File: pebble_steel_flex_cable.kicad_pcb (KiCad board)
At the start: 2 copper layers, 80 x 19 mm, 33 parts, among them J1 505551-1620, SW1 Select, SW2 DOWN, SW3 UP, SW4 BACK, U1 IS31FL3199-QFLS2-TR

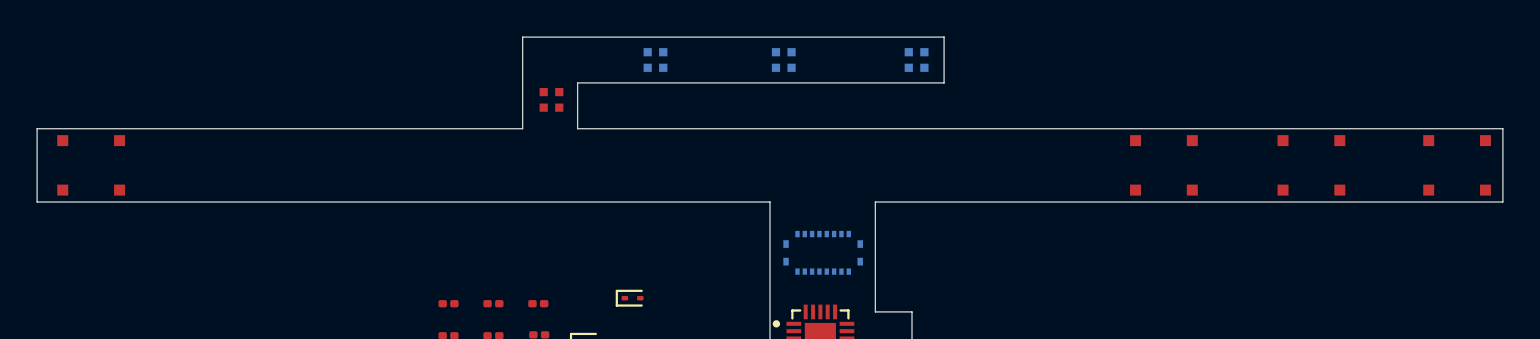
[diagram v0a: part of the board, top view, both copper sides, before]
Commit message: added the buttons and the battery connections
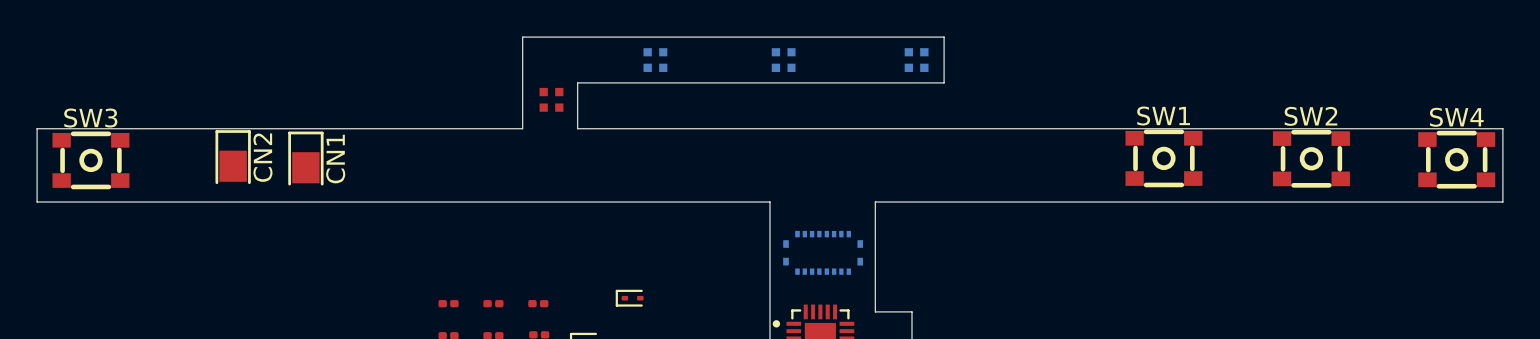
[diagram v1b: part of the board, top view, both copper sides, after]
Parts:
- added CN1: ~, S7121-42R:SMD_L2.7-W1.5, F.Cu at (108.7, 58.1)
- added CN2: ~, S7121-42R:SMD_L2.7-W1.5, F.Cu at (104.7, 58.0)
- SW1: value Select -> UP; footprint button-TL3315NF250Q:SW_TL3315NF250Q -> SKSHAAE010:SW-SMD_SKSHAAE010
- SW2: value DOWN -> Select; footprint button-TL3315NF250Q:SW_TL3315NF250Q -> SKSHAAE010:SW-SMD_SKSHAAE010
- SW3: value UP -> Back; footprint button-TL3315NF250Q:SW_TL3315NF250Q -> SKSHAAE010:SW-SMD_SKSHAAE010
- SW4: value BACK -> Down; footprint button-TL3315NF250Q:SW_TL3315NF250Q -> SKSHAAE010:SW-SMD_SKSHAAE010
- moved SW4 74.5 mm to (171.5, 57.7)
- moved SW3 58.6 mm to (96.9, 57.7)
- moved SW1 16.0 mm to (155.5, 57.6)
- moved SW2 0.36 mm to (163.6, 57.6)
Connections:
- SW1 pad 2: Net-(D3-A2) -> unconnected-(SW1-Pad2)
- SW1 pad 3: (no net) -> unconnected-(SW1-Pad3)
- SW1 pad 4: (no net) -> Net-(D3-A2)
- SW2 pad 2: Net-(D4-A2) -> unconnected-(SW2-Pad2)
- SW2 pad 3: (no net) -> unconnected-(SW2-Pad3)
- SW2 pad 4: (no net) -> Net-(D4-A2)
- SW3 pad 2: Net-(D2-A2) -> unconnected-(SW3-Pad2)
- SW3 pad 3: (no net) -> unconnected-(SW3-Pad3)
- SW3 pad 4: (no net) -> Net-(D2-A2)
- SW4 pad 2: Net-(D5-A2) -> unconnected-(SW4-Pad2)
- SW4 pad 3: (no net) -> unconnected-(SW4-Pad3)
- SW4 pad 4: (no net) -> Net-(D5-A2)

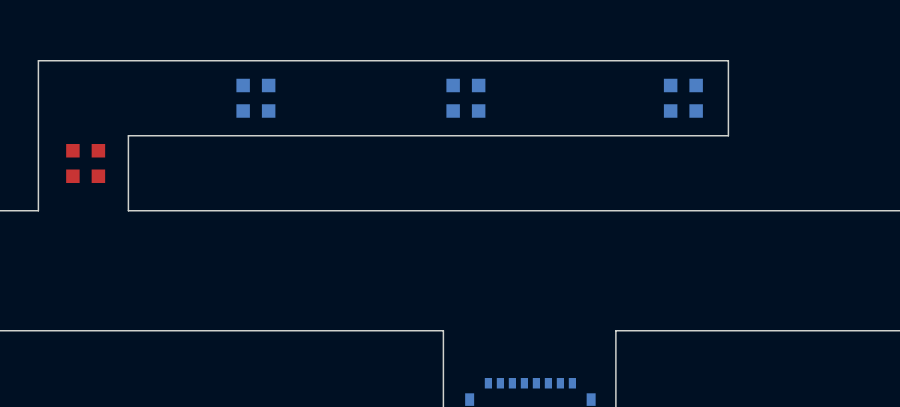
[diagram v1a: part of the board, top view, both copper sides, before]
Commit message: added the LED part
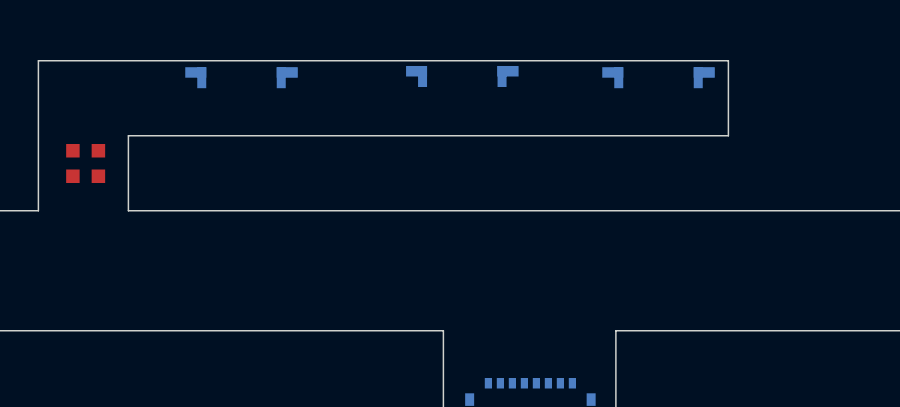
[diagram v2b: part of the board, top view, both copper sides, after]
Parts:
- CN1: value ~ -> 5v
- CN2: value ~ -> GND
- D6, D7, D8: footprint footprints:led_SML-LX0404SIUPGUSB -> LTW-020ZDCG:LTW-020ZDCG
- moved D8 3.75 mm to (141.2, 48.6)
- moved D7 3.70 mm to (134.6, 48.5)
- moved D6 3.69 mm to (127.3, 48.6)

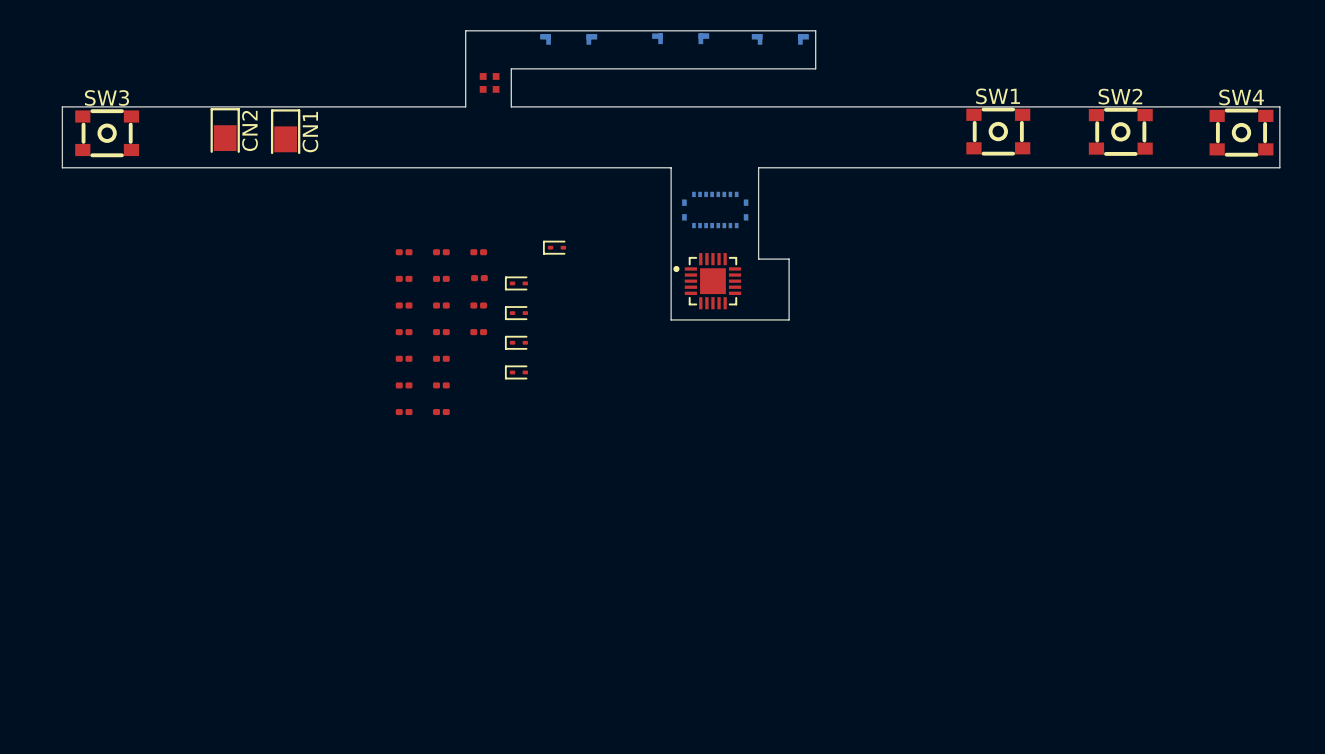
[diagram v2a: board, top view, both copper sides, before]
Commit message: got the outline almost there
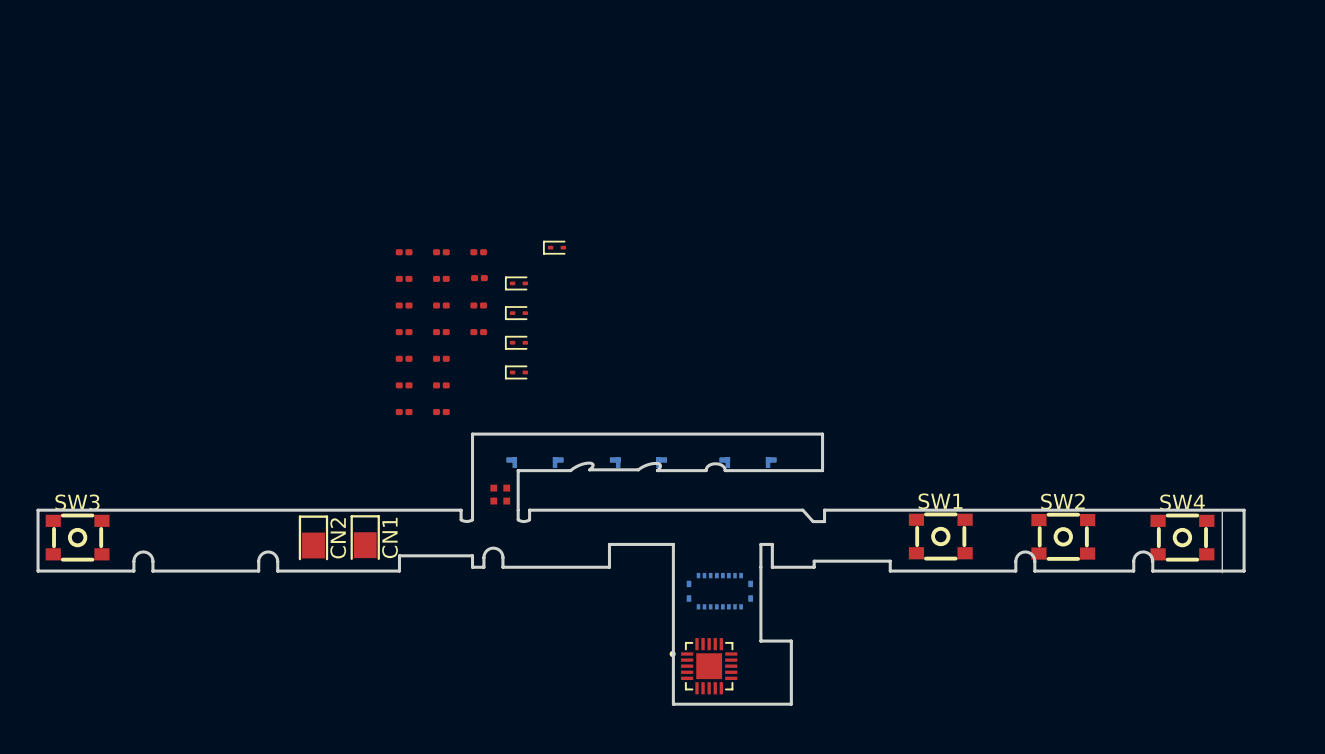
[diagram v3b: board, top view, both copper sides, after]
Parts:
- moved D7 28.0 mm to (131.8, 76.4)
- moved D6 27.9 mm to (125.0, 76.4)
- moved D8 27.9 mm to (139.1, 76.4)
- moved CN2 27.4 mm to (110.5, 84.8)
- moved CN1 27.2 mm to (113.9, 84.8)
- moved D10 27.1 mm to (122.8, 81.5)
- moved SW4 26.9 mm to (167.6, 84.3)
- moved SW1 26.9 mm to (151.7, 84.2)
- moved SW2 26.9 mm to (159.8, 84.2)
- moved SW3 26.6 mm to (95.0, 84.3)
- moved U1 25.3 mm to (136.5, 92.8)
- moved J1 25.1 mm to (137.2, 87.8)
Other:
- board size 80 x 19 mm -> 79.2 x 17.8 mm

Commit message: got the flex layed out
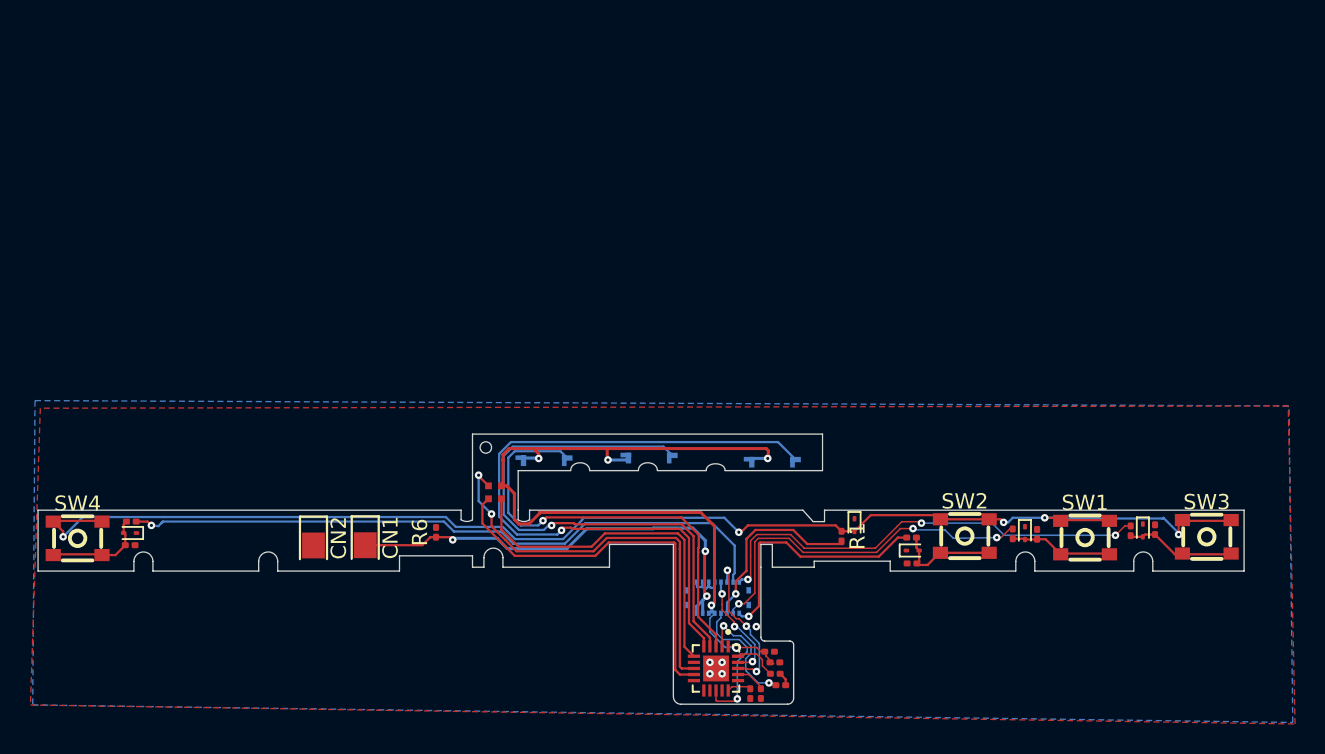
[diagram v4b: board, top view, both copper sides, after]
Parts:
- removed C5, C6: C, Capacitor_SMD:C_0201_0603Metric
- SW1: value UP -> Select
- SW2: value Select -> UP
- SW3: value Back -> Down
- SW4: value Down -> Back
- moved SW3 74.2 mm to (169.2, 84.2)
- moved SW4 72.6 mm to (95.0, 84.3)
- moved C4 51.0 mm to (165.8, 83.8), turned to 90 degrees
- moved R5 46.6 mm to (164.2, 83.9), turned to -90 degrees
- moved C3 44.2 mm to (158.1, 84.1), turned to 90 degrees
- moved D5 42.3 mm to (165.0, 83.8), turned to -90 degrees
- moved R4 38.4 mm to (156.4, 84.1), turned to -90 degrees
- moved C2 38.3 mm to (149.8, 86.0), turned to 180 degrees
- moved C9 36.1 mm to (141.2, 94.0)
- moved D4 35.5 mm to (157.2, 84.0), turned to -90 degrees
- moved C10 33.4 mm to (140.8, 92.5)
- moved R3 32.5 mm to (149.8, 84.3)
- moved C11 31.3 mm to (140.5, 91.8)
- moved R7 31.1 mm to (139.2, 94.6), turned to 90 degrees
- moved D2 30.4 mm to (98.4, 84.0), turned to 180 degrees
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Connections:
- R2 pad 1: Net-(J1-Pad2) -> Net-(J1-Pad4)
- R5 pad 1: Net-(J1-Pad4) -> Net-(J1-Pad2)
- R6 pad 1: +3.3V -> +5V
- SW1 pad 2: unconnected-(SW1-Pad2) -> Net-(D4-A2)
- SW1 pad 3: unconnected-(SW1-Pad3) -> Net-(D1-A2)
- SW1 pad 4: Net-(D3-A2) -> Net-(D4-A2)
- SW2 pad 2: unconnected-(SW2-Pad2) -> Net-(D3-A2)
- SW2 pad 3: unconnected-(SW2-Pad3) -> Net-(D1-A2)
- SW2 pad 4: Net-(D4-A2) -> Net-(D3-A2)
- SW3 pad 2: unconnected-(SW3-Pad2) -> Net-(D5-A2)
- SW3 pad 3: unconnected-(SW3-Pad3) -> Net-(D1-A2)
- SW3 pad 4: Net-(D2-A2) -> Net-(D5-A2)
- SW4 pad 2: unconnected-(SW4-Pad2) -> Net-(D2-A2)
- SW4 pad 3: unconnected-(SW4-Pad3) -> Net-(D1-A2)
- SW4 pad 4: Net-(D5-A2) -> Net-(D2-A2)
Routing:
- net Net-(D1-A2): track 0.00 -> 90.3 mm, vias 0 -> 5
- net +3.3V: track 0.00 -> 55.9 mm, vias 0 -> 5
- net /LED3: track 0.00 -> 45.4 mm, vias 0 -> 1
- net Net-(J1-Pad4): track 0.00 -> 43.9 mm, vias 0 -> 1
- net /LED2: track 0.00 -> 36.6 mm, vias 0 -> 1
- net Net-(J1-Pad2): track 0.00 -> 30.3 mm, vias 0 -> 3
- net +5V: track 0.00 -> 30.0 mm, vias 0 -> 3
- net /LED1: track 0.00 -> 29.4 mm, vias 0 -> 1
- net /LED_B: track 0.00 -> 27.5 mm, vias 0 -> 2
- net /LED_G: track 0.00 -> 25.4 mm
- net Net-(J1-Pad3): track 0.00 -> 24.3 mm, vias 0 -> 3
- net /LED_R: track 0.00 -> 23.0 mm
- net Net-(J1-Pad1): track 0.00 -> 16.6 mm, vias 0 -> 1
- net Net-(J1-Pad5): track 0.00 -> 12.6 mm, vias 0 -> 1
- net /SCL: track 0.00 -> 10.0 mm, vias 0 -> 3
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- added copper zone on B.Cu, net GND
- added copper zone on F.Cu, net GND
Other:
- outline, holes or cut-outs redrawn

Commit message: send for fit test
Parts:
- moved D6 0.33 mm to (140.6, 76.3)
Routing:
- net GND: vias 5 -> 7
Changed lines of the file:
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@@
 		(tags "resistor")
 		(property "Reference" "R2"
-			(at 0 -1.05 360)
+			(at 0 -1.05 0)
 			(layer "F.SilkS")
 			(hide yes)
@@
 		)
 		(property "Value" "R"
-			(at 0 1.05 360)
+			(at 0 1.05 0)
 			(layer "F.Fab")
 			(hide yes)
@@
 		(tags "capacitor")
 		(property "Reference" "C1"
-			(at 0 -1.05 360)
+			(at 0 -1.05 0)
 			(layer "F.SilkS")
 			(hide yes)
@@
 		)
 		(property "Value" "C"
-			(at 0 1.05 360)
+			(at 0 1.05 0)
 			(layer "F.Fab")
 			(hide yes)
@@
 		(tags "Diode SOD923")
 		(property "Reference" "D2"
-			(at 0 -1.2 360)
+			(at 0 -1.2 0)
 			(layer "F.SilkS")
 			(hide yes)
@@
 		)
 		(property "Value" "ESD9B3.3ST5G"
-			(at 0 1.2 360)
+			(at 0 1.2 0)
 			(layer "F.Fab")
 			(hide yes)
@@
 	(footprint "LTW-020ZDCG:LTW-020ZDCG"
 		(layer "B.Cu")
-		(at 140.575 76.65 180)
+		(at 140.6 76.325 180)
 		(property "Reference" "D6"
 			(at 0 0.5 0)
@@
 	)
 	(via
+		(at 141.05 94.85)
+		(size 0.5)
+		(drill 0.2)
+		(layers "F.Cu" "B.Cu")
+		(free yes)
+		(net 1)
+	)
+	(via
 		(at 137.35 92.5)
 		(size 0.5)
@@
 	)
 	(via
+		(at 141.6 91.6)
+		(size 0.5)
+		(drill 0.2)
+		(layers "F.Cu" "B.Cu")
+		(free yes)
+		(net 1)
+	)
+	(via
 		(at 137.35 93.25)
 		(size 0.5)
@@
 	)
 	(segment
-		(start 137 95.05)
-		(end 136.95 95)
+		(start 136.95 95)
+		(end 136.95 94.35)
 		(width 0.1)
 		(layer "F.Cu")
@@
 	)
 	(segment
-		(start 138.35 94.9)
-		(end 138.2 95.05)
+		(start 137.95 95.05)
+		(end 137 95.05)
 		(width 0.1)
 		(layer "F.Cu")
@@
 	)
 	(segment
-		(start 136.95 95)
-		(end 136.95 94.35)
+		(start 138.45 94.55)
+		(end 137.95 95.05)
 		(width 0.1)
 		(layer "F.Cu")
@@
 	)
 	(segment
-		(start 138.2 95.05)
-		(end 137 95.05)
+		(start 137 95.05)
+		(end 136.95 95)
 		(width 0.1)
 		(layer "F.Cu")
@@
 	)
 	(via
-		(at 138.35 94.9)
+		(at 138.45 94.55)
 		(size 0.5)
 		(drill 0.2)
@@
 	)
 	(segment
-		(start 137 90.596446)
-		(end 137.403554 91)
-		(width 0.1)
-		(layer "B.Cu")
-		(net 17)
-	)
-	(segment
-		(start 138.35 94.95)
-		(end 138.3 95)
+		(start 137.275 89.57)
+		(end 137.275 89.275)
 		(width 0.1)
 		(layer "B.Cu")
@@
 	)
 	(segment
-		(start 137.275 89.275)
-		(end 137.275 89.57)
+		(start 139 91.521394)
+		(end 138.478606 91)
 		(width 0.1)
 		(layer "B.Cu")
@@
 	)
 	(segment
-		(start 137 89.845)
+		(start 137.403554 91)
 		(end 137 90.596446)
 		(width 0.1)
@@
 	)
 	(segment
-		(start 139 91.521394)
+		(start 138.45 92.35)
 		(end 139 91.8)
 		(width 0.1)
@@
 	)
 	(segment
-		(start 138.35 94.9)
-		(end 138.35 94.95)
-		(width 0.1)
-		(layer "B.Cu")
-		(net 17)
-	)
-	(segment
-		(start 137.275 89.57)
-		(end 137 89.845)
+		(start 137 89.845)
+		(end 137.275 89.57)
 		(width 0.1)
 		(layer "B.Cu")
@@
 	(segment
 		(start 138.478606 91)
-		(end 139 91.521394)
+		(end 137.403554 91)
 		(width 0.1)
 		(layer "B.Cu")
@@
 	)
 	(segment
-		(start 139 91.8)
-		(end 138.35 92.45)
+		(start 137 90.596446)
+		(end 137 89.845)
 		(width 0.1)
 		(layer "B.Cu")
@@
 	)
 	(segment
-		(start 138.35 92.45)
-		(end 138.35 94.9)
+		(start 138.45 94.55)
+		(end 138.45 92.35)
 		(width 0.1)
 		(layer "B.Cu")
@@
 	)
 	(segment
-		(start 137.403554 91)
-		(end 138.478606 91)
+		(start 139 91.8)
+		(end 139 91.521394)
 		(width 0.1)
 		(layer "B.Cu")

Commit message: not sure what changed
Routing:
- net GND: track 3.53 -> 7.06 mm
